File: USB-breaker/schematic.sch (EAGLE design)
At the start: 15 parts, among them K1 G6K-2P, K3 G6K-2P, X1 PN87520-S, X2 PN87520-S

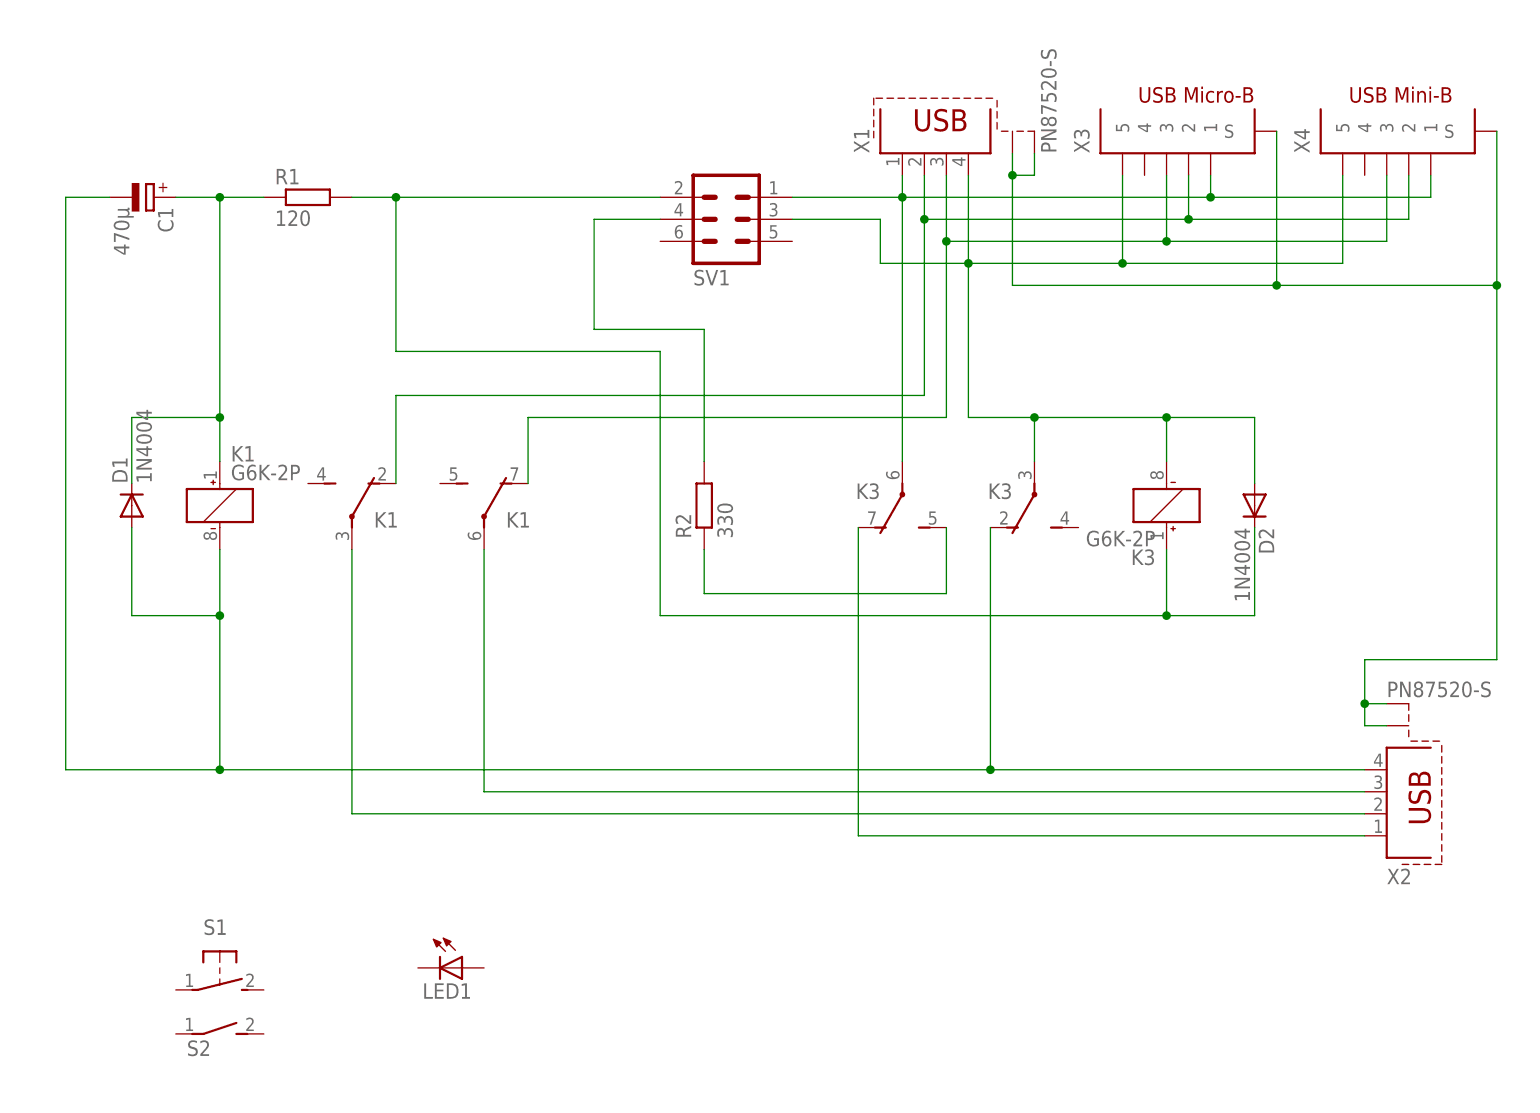
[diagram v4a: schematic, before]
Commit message: Bugfix: Connect the delayed relay to GND_IN instead of the (already disconnected off) GND_OUT.
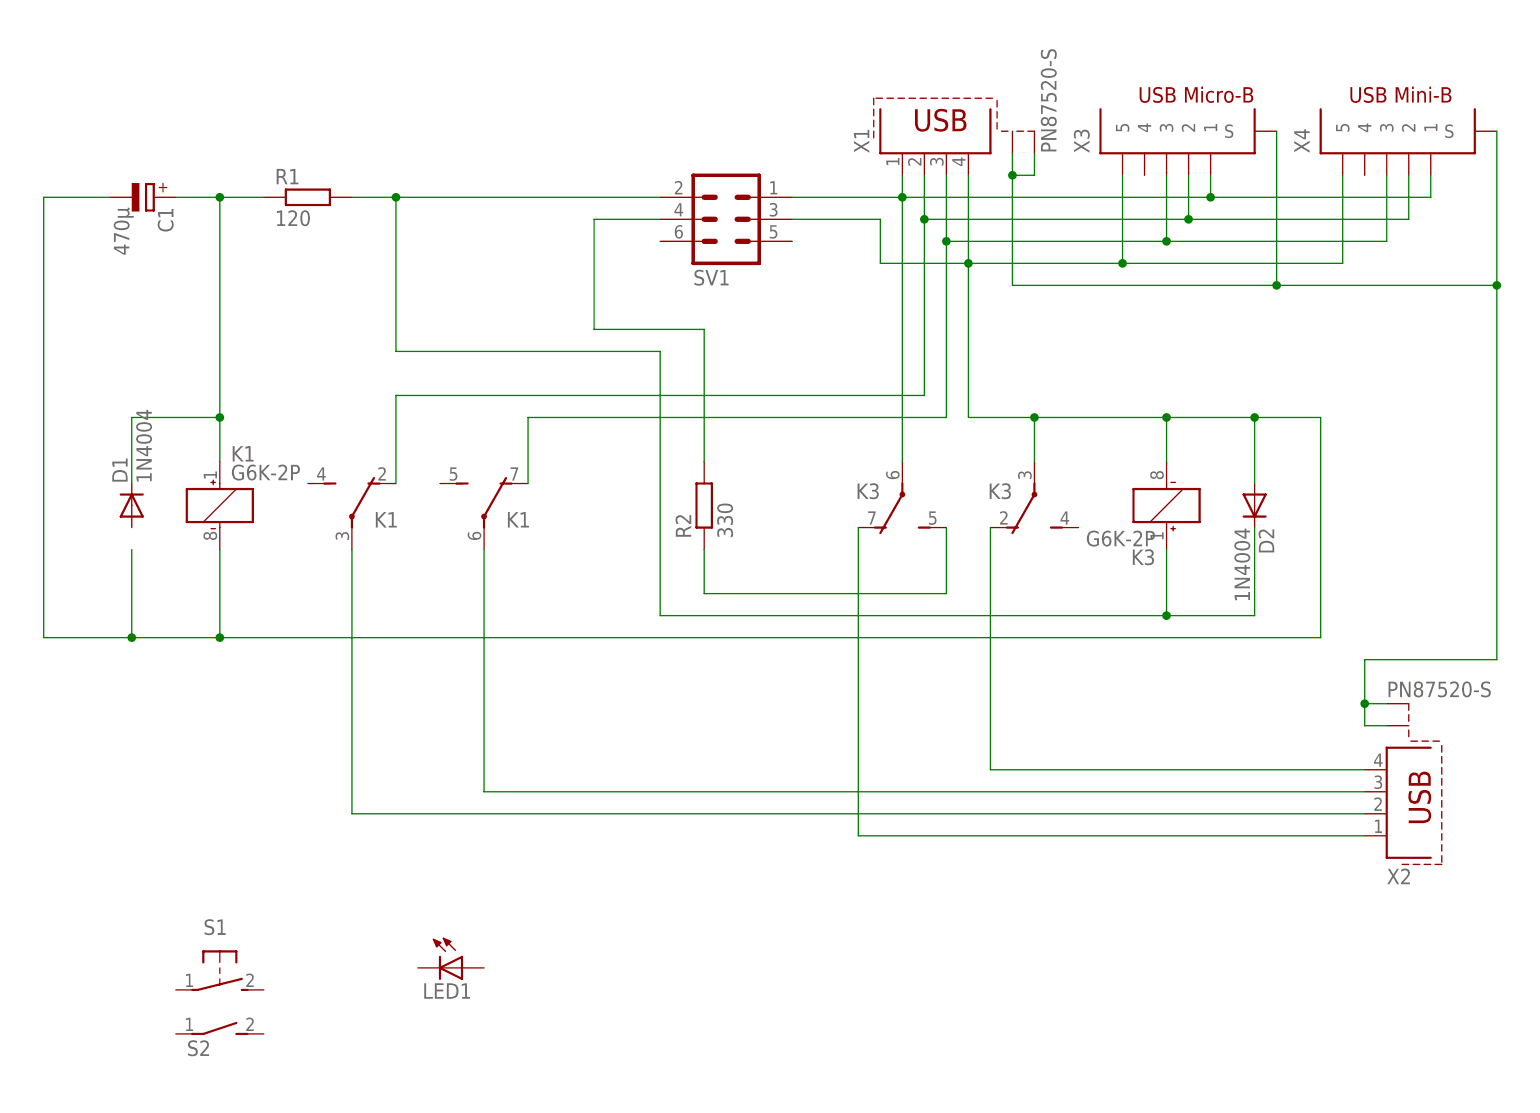
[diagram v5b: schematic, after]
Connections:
- removed net GND-OUT: C1.-, D1.A, K11.-, K32.O, X2.4
- new net N$1: K32.O, X2.4
- net GND-IN: now also C1.-, K11.-
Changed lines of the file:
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@@
 <wire x1="106.68" y1="106.68" x2="106.68" y2="101.6" width="0.1524" layer="91"/>
 <wire x1="106.68" y1="101.6" x2="116.84" y2="101.6" width="0.1524" layer="91"/>
-</segment>
-</net>
-<net name="GND-OUT" class="0">
-<segment>
-<wire x1="30.48" y1="68.58" x2="30.48" y2="60.96" width="0.1524" layer="91"/>
-<wire x1="30.48" y1="60.96" x2="30.48" y2="43.18" width="0.1524" layer="91"/>
+<wire x1="149.86" y1="83.82" x2="157.48" y2="83.82" width="0.1524" layer="91"/>
+<wire x1="157.48" y1="83.82" x2="157.48" y2="58.42" width="0.1524" layer="91"/>
+<junction x="149.86" y="83.82"/>
+<wire x1="157.48" y1="58.42" x2="30.48" y2="58.42" width="0.1524" layer="91"/>
+<pinref part="K1" gate="1" pin="-"/>
+<wire x1="30.48" y1="68.58" x2="30.48" y2="58.42" width="0.1524" layer="91"/>
+<wire x1="30.48" y1="58.42" x2="20.32" y2="58.42" width="0.1524" layer="91"/>
+<junction x="30.48" y="58.42"/>
+<wire x1="20.32" y1="68.58" x2="20.32" y2="58.42" width="0.1524" layer="91"/>
+<wire x1="20.32" y1="58.42" x2="10.16" y2="58.42" width="0.1524" layer="91"/>
+<wire x1="10.16" y1="58.42" x2="10.16" y2="109.22" width="0.1524" layer="91"/>
+<junction x="20.32" y="58.42"/>
 <pinref part="C1" gate="G$1" pin="-"/>
-<wire x1="17.78" y1="109.22" x2="12.7" y2="109.22" width="0.1524" layer="91"/>
-<wire x1="12.7" y1="109.22" x2="12.7" y2="43.18" width="0.1524" layer="91"/>
-<wire x1="12.7" y1="43.18" x2="30.48" y2="43.18" width="0.1524" layer="91"/>
-<pinref part="D1" gate="1" pin="A"/>
-<wire x1="20.32" y1="71.12" x2="20.32" y2="60.96" width="0.1524" layer="91"/>
-<wire x1="20.32" y1="60.96" x2="30.48" y2="60.96" width="0.1524" layer="91"/>
-<junction x="30.48" y="60.96"/>
-<pinref part="K1" gate="1" pin="-"/>
-<wire x1="119.38" y1="43.18" x2="162.56" y2="43.18" width="0.1524" layer="91"/>
-<wire x1="119.38" y1="71.12" x2="119.38" y2="43.18" width="0.1524" layer="91"/>
-<wire x1="30.48" y1="43.18" x2="119.38" y2="43.18" width="0.1524" layer="91"/>
-<junction x="30.48" y="43.18"/>
-<junction x="119.38" y="43.18"/>
-<pinref part="K3" gate="2" pin="O"/>
-<pinref part="X2" gate="G$1" pin="4"/>
+<wire x1="10.16" y1="109.22" x2="17.78" y2="109.22" width="0.1524" layer="91"/>
 </segment>
 </net>
@@
 </segment>
 </net>
+<net name="N$1" class="0">
+<segment>
+<pinref part="X2" gate="G$1" pin="4"/>
+<wire x1="119.38" y1="43.18" x2="162.56" y2="43.18" width="0.1524" layer="91"/>
+<pinref part="K3" gate="2" pin="O"/>
+<wire x1="119.38" y1="71.12" x2="119.38" y2="43.18" width="0.1524" layer="91"/>
+</segment>
+</net>

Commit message: Completed front panel components.
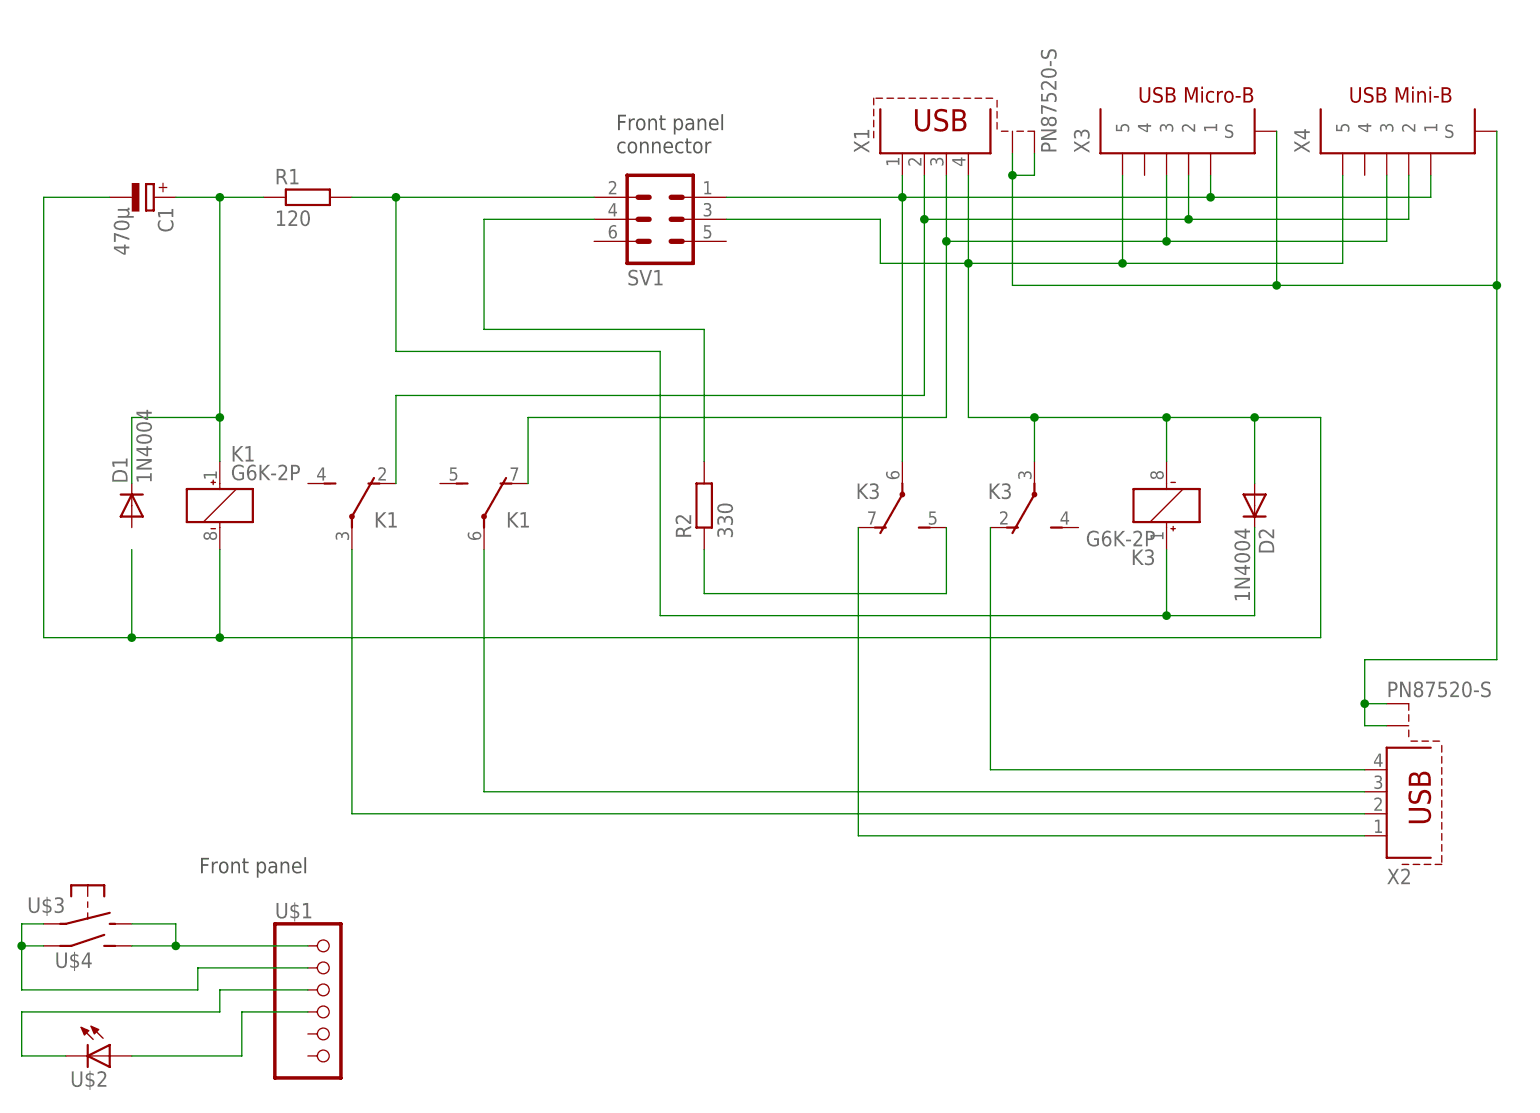
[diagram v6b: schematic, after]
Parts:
- removed LED1: (no value), led:LED3MM
- removed S1: (no value), switch-omron:31-XX
- removed S2: (no value), switch-dil:DS01E
- added U$1: EXTERNAL_CONNECTOR_6, mibe:EXTERNAL_CONNECTOR_6
- added U$2: EXTERNAL_LED, mibe:EXTERNAL_LED
- added U$3: EXTERNAL_PUSH_BUTTON, mibe:EXTERNAL_PUSH_BUTTON
- added U$4: EXTERNAL_SWITCH, mibe:EXTERNAL_SWITCH
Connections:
- net ENABLE: now also U$1.2, U$3.P, U$4.1
- net GND-IN: now also U$1.3, U$2.C
- net LED: now also U$1.4, U$2.A
- net VCC-IN: now also U$1.1, U$3.S, U$4.2
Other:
- note added: "Front panel"
- note added: "Front panel connector"
- moved on the sheet: SV1
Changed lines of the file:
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@@
 <parts>
 <part name="FRAME1" library="frames" deviceset="DINA5_L" device=""/>
-<part name="S1" library="switch-omron" deviceset="31-XX" device=""/>
 <part name="R1" library="resistor" deviceset="R-EU_" device="0207/10" value="120"/>
 <part name="C1" library="resistor" deviceset="CPOL-EU" device="E3.5-8" value="470µ"/>
 <part name="D1" library="diode" deviceset="1N4004" device=""/>
-<part name="S2" library="switch-dil" deviceset="DS01E" device=""/>
-<part name="LED1" library="led" deviceset="LED" device="3MM"/>
 <part name="R2" library="resistor" deviceset="R-EU_" device="0207/10" value="330"/>
 <part name="D2" library="diode" deviceset="1N4004" device=""/>
@@
 <part name="X1" library="con-berg" deviceset="PN87520-S" device=""/>
 <part name="SV1" library="con-harting-ml" deviceset="ML6" device=""/>
+<part name="U$1" library="mibe" deviceset="EXTERNAL_CONNECTOR_6" device=""/>
+<part name="U$2" library="mibe" deviceset="EXTERNAL_LED" device=""/>
+<part name="U$3" library="mibe" deviceset="EXTERNAL_PUSH_BUTTON" device=""/>
+<part name="U$4" library="mibe" deviceset="EXTERNAL_SWITCH" device=""/>
 </parts>
 <sheets>
 <sheet>
 <plain>
+<text x="40.64" y="33.02" size="1.778" layer="97" rot="R180">Front panel</text>
+<text x="76.2" y="114.3" size="1.778" layer="97">Front panel
+connector</text>
 </plain>
 <instances>
 <instance part="FRAME1" gate="G$1" x="0" y="0"/>
-<instance part="S1" gate="1" x="30.48" y="17.78" rot="R270"/>
 <instance part="R1" gate="G$1" x="40.64" y="109.22"/>
 <instance part="C1" gate="G$1" x="22.86" y="109.22" rot="R270"/>
 <instance part="D1" gate="1" x="20.32" y="73.66" rot="R90"/>
-<instance part="S2" gate="1" x="30.48" y="12.7" rot="R270"/>
-<instance part="LED1" gate="G$1" x="58.42" y="20.32" rot="R270"/>
 <instance part="R2" gate="G$1" x="86.36" y="73.66" rot="R90"/>
 <instance part="D2" gate="1" x="149.86" y="73.66" rot="R270"/>
@@
 <instance part="X2" gate="G$1" x="165.1" y="40.64" rot="MR180"/>
 <instance part="X1" gate="G$1" x="114.3" y="114.3" rot="R90"/>
-<instance part="SV1" gate="1" x="88.9" y="106.68" rot="MR180"/>
+<instance part="SV1" gate="1" x="81.28" y="106.68" rot="MR180"/>
+<instance part="U$1" gate="G$1" x="43.18" y="15.24" smashed="yes">
+<attribute name="NAME" x="36.83" y="26.035" size="1.778" layer="95"/>
+</instance>
+<instance part="U$2" gate="G$1" x="15.24" y="10.16" smashed="yes" rot="R270">
+<attribute name="NAME" x="13.208" y="6.604" size="1.778" layer="95"/>
+</instance>
+<instance part="U$3" gate="G$1" x="15.24" y="25.4" smashed="yes" rot="R270">
+<attribute name="NAME" x="8.255" y="26.67" size="1.778" layer="95"/>
+</instance>
+<instance part="U$4" gate="G$1" x="15.24" y="22.86" smashed="yes" rot="R270">
+<attribute name="NAME" x="11.43" y="20.32" size="1.778" layer="95"/>
+</instance>
 </instances>
 <busses>
@@
 <pinref part="X1" gate="G$1" pin="1"/>
 <pinref part="SV1" gate="1" pin="1"/>
-<wire x1="109.22" y1="109.22" x2="96.52" y2="109.22" width="0.1524" layer="91"/>
+<wire x1="109.22" y1="109.22" x2="88.9" y2="109.22" width="0.1524" layer="91"/>
+</segment>
+<segment>
+<pinref part="U$1" gate="G$1" pin="1"/>
+<pinref part="U$4" gate="G$1" pin="2"/>
+<wire x1="40.64" y1="22.86" x2="25.4" y2="22.86" width="0.1524" layer="91"/>
+<wire x1="25.4" y1="22.86" x2="20.32" y2="22.86" width="0.1524" layer="91"/>
+<pinref part="U$3" gate="G$1" pin="S"/>
+<wire x1="20.32" y1="25.4" x2="25.4" y2="25.4" width="0.1524" layer="91"/>
+<wire x1="25.4" y1="25.4" x2="25.4" y2="22.86" width="0.1524" layer="91"/>
+<junction x="25.4" y="22.86"/>
 </segment>
 </net>
@@
 <pinref part="X1" gate="G$1" pin="4"/>
 <pinref part="SV1" gate="1" pin="3"/>
-<wire x1="96.52" y1="106.68" x2="106.68" y2="106.68" width="0.1524" layer="91"/>
+<wire x1="88.9" y1="106.68" x2="106.68" y2="106.68" width="0.1524" layer="91"/>
 <wire x1="106.68" y1="106.68" x2="106.68" y2="101.6" width="0.1524" layer="91"/>
 <wire x1="106.68" y1="101.6" x2="116.84" y2="101.6" width="0.1524" layer="91"/>
@@
 <wire x1="10.16" y1="109.22" x2="17.78" y2="109.22" width="0.1524" layer="91"/>
 </segment>
+<segment>
+<pinref part="U$1" gate="G$1" pin="3"/>
+<wire x1="40.64" y1="17.78" x2="30.48" y2="17.78" width="0.1524" layer="91"/>
+<pinref part="U$2" gate="G$1" pin="C"/>
+<wire x1="7.62" y1="15.24" x2="7.62" y2="10.16" width="0.1524" layer="91"/>
+<wire x1="7.62" y1="10.16" x2="12.7" y2="10.16" width="0.1524" layer="91"/>
+<wire x1="30.48" y1="17.78" x2="30.48" y2="15.24" width="0.1524" layer="91"/>
+<wire x1="30.48" y1="15.24" x2="7.62" y2="15.24" width="0.1524" layer="91"/>
+</segment>
 </net>
 <net name="VCC-OUT" class="0">
@@
 <pinref part="K3" gate="1" pin="+"/>
 <pinref part="SV1" gate="1" pin="2"/>
-<wire x1="81.28" y1="109.22" x2="50.8" y2="109.22" width="0.1524" layer="91"/>
+<wire x1="73.66" y1="109.22" x2="50.8" y2="109.22" width="0.1524" layer="91"/>
 <junction x="50.8" y="109.22"/>
+</segment>
+<segment>
+<pinref part="U$4" gate="G$1" pin="1"/>
+<wire x1="10.16" y1="22.86" x2="7.62" y2="22.86" width="0.1524" layer="91"/>
+<wire x1="7.62" y1="22.86" x2="7.62" y2="17.78" width="0.1524" layer="91"/>
+<pinref part="U$1" gate="G$1" pin="2"/>
+<wire x1="27.94" y1="20.32" x2="40.64" y2="20.32" width="0.1524" layer="91"/>
+<wire x1="7.62" y1="22.86" x2="7.62" y2="25.4" width="0.1524" layer="91"/>
+<junction x="7.62" y="22.86"/>
+<pinref part="U$3" gate="G$1" pin="P"/>
+<wire x1="7.62" y1="25.4" x2="10.16" y2="25.4" width="0.1524" layer="91"/>
+<wire x1="27.94" y1="20.32" x2="27.94" y2="17.78" width="0.1524" layer="91"/>
+<wire x1="27.94" y1="17.78" x2="7.62" y2="17.78" width="0.1524" layer="91"/>
 </segment>
 </net>
@@
 <pinref part="R2" gate="G$1" pin="2"/>
 <wire x1="86.36" y1="78.74" x2="86.36" y2="93.98" width="0.1524" layer="91"/>
-<wire x1="86.36" y1="93.98" x2="73.66" y2="93.98" width="0.1524" layer="91"/>
-<wire x1="73.66" y1="93.98" x2="73.66" y2="106.68" width="0.1524" layer="91"/>
+<wire x1="86.36" y1="93.98" x2="60.96" y2="93.98" width="0.1524" layer="91"/>
+<wire x1="60.96" y1="93.98" x2="60.96" y2="106.68" width="0.1524" layer="91"/>
 <pinref part="SV1" gate="1" pin="4"/>
-<wire x1="73.66" y1="106.68" x2="81.28" y2="106.68" width="0.1524" layer="91"/>
+<wire x1="60.96" y1="106.68" x2="73.66" y2="106.68" width="0.1524" layer="91"/>
+</segment>
+<segment>
+<pinref part="U$2" gate="G$1" pin="A"/>
+<wire x1="20.32" y1="10.16" x2="33.02" y2="10.16" width="0.1524" layer="91"/>
+<wire x1="33.02" y1="10.16" x2="33.02" y2="15.24" width="0.1524" layer="91"/>
+<pinref part="U$1" gate="G$1" pin="4"/>
+<wire x1="33.02" y1="15.24" x2="40.64" y2="15.24" width="0.1524" layer="91"/>
 </segment>
 </net>
@@
 </schematic>
 </drawing>
+<compatibility>
+<note version="6.3" minversion="6.2.2" severity="warning">
+Since Version 6.2.2 text objects can contain more than one line,
+which will not be processed correctly with this version.
+</note>
+</compatibility>
 </eagle>
